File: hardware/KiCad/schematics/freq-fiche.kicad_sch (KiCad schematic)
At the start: 20 parts, among them J1 AudioJack2, J2 AudioJack2, J3 Barrel_Jack_Switch_Pin3Ring, SW1 SW_SPST, SW2 SW_SPST, SW3 SW_SPDT

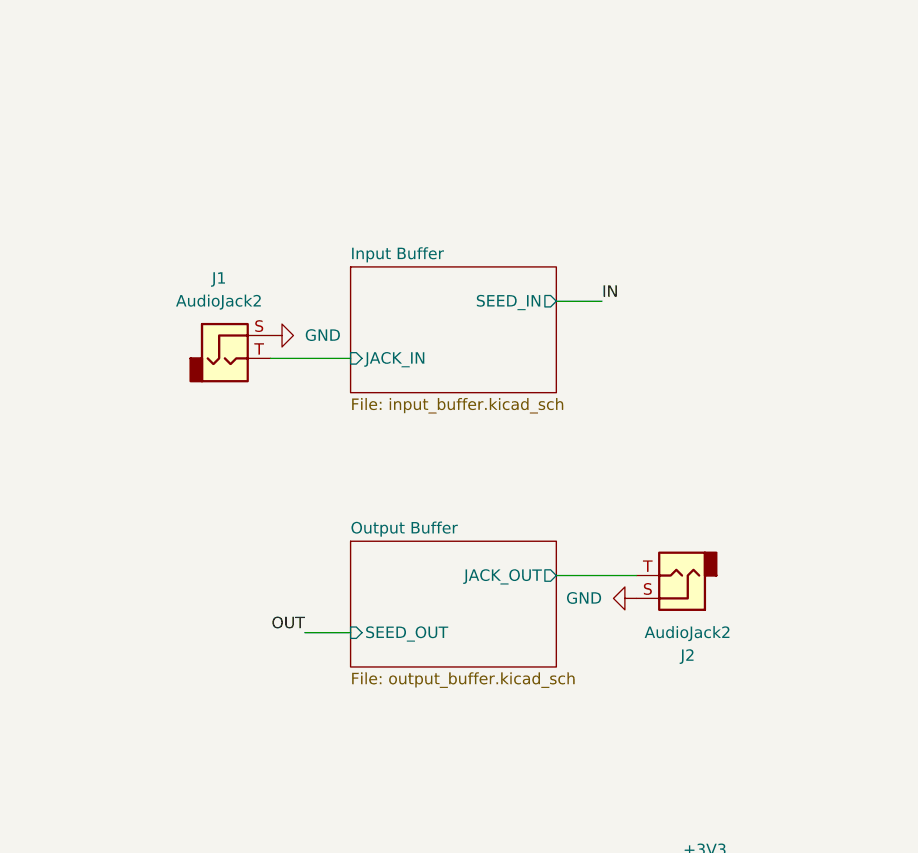
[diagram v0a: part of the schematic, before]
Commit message: Footprint assignments for most components; file organization.
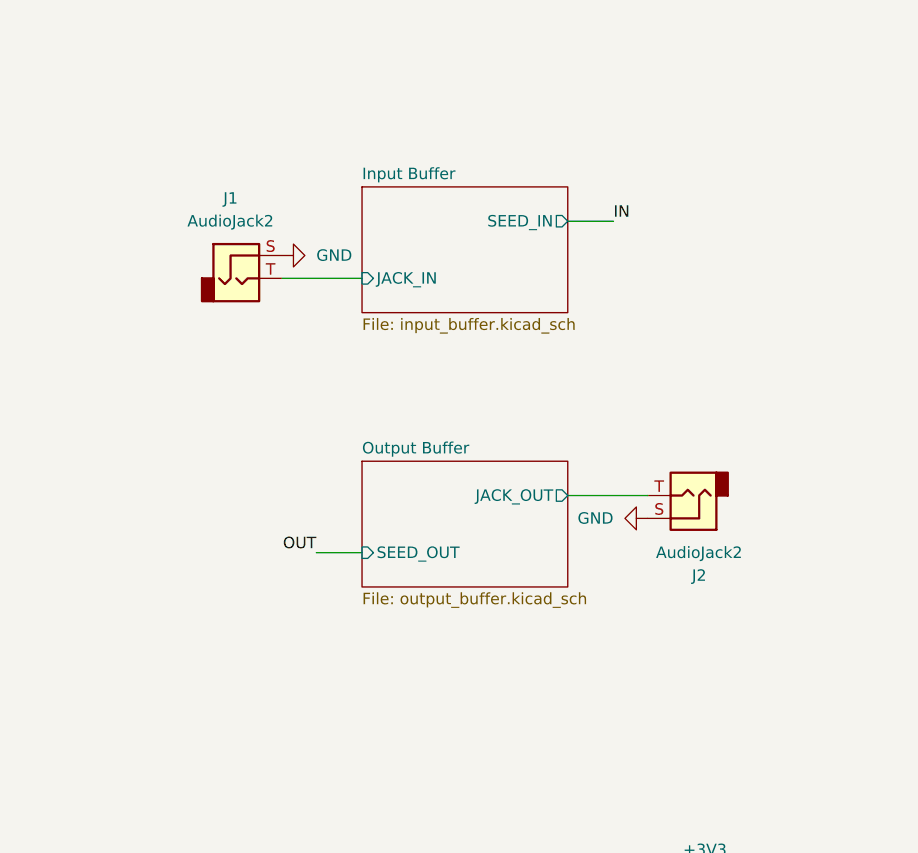
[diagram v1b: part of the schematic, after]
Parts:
- C1: footprint (none) -> Capacitor_THT_Custom:C_Rect_L4.0mm_W2.6mm_P2.50mm
- D1, D2: footprint (none) -> LED_THT:LED_D5.0mm
- J1, J2, SW1, SW2: footprint (none) -> Connector_Wire:SolderWire-0.5sqmm_1x02_P4.6mm_D0.9mm_OD2.1mm
- R1, R2, R3, R4: footprint (none) -> Resistor_THT:R_Axial_DIN0207_L6.3mm_D2.5mm_P7.62mm_Horizontal
- RV1, RV2, RV3, RV4, RV5: footprint (none) -> Potentiometer_THT_Custom:Potentiometer_P160KN
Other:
- moved on the sheet: J1, J2
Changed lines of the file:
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@@
 	(wire
 		(pts
-			(xy 109.22 85.09) (xy 118.11 85.09)
+			(xy 110.49 76.2) (xy 119.38 76.2)
 		)
 		(stroke
@@
 	(wire
 		(pts
-			(xy 81.28 91.44) (xy 86.36 91.44)
+			(xy 82.55 82.55) (xy 87.63 82.55)
 		)
 		(stroke
@@
 	(wire
 		(pts
-			(xy 109.22 54.61) (xy 114.3 54.61)
+			(xy 110.49 45.72) (xy 115.57 45.72)
 		)
 		(stroke
@@
 	(wire
 		(pts
-			(xy 77.47 60.96) (xy 86.36 60.96)
+			(xy 78.74 52.07) (xy 87.63 52.07)
 		)
 		(stroke
@@
 	)
 	(label "IN"
-		(at 114.3 54.61 0)
+		(at 115.57 45.72 0)
 		(effects
 			(font
@@
 	)
 	(label "OUT"
-		(at 81.28 91.44 180)
+		(at 82.55 82.55 180)
 		(effects
 			(font
@@
 			)
 		)
-		(property "Footprint" ""
+		(property "Footprint" "Potentiometer_THT_Custom:Potentiometer_P160KN"
 			(at 116.84 172.72 0)
 			(hide yes)
@@
 			)
 		)
-		(property "Footprint" ""
+		(property "Footprint" "LED_THT:LED_D5.0mm"
 			(at 153.67 138.43 0)
 			(hide yes)
@@
 			)
 		)
-		(property "Footprint" ""
+		(property "Footprint" "Resistor_THT:R_Axial_DIN0207_L6.3mm_D2.5mm_P7.62mm_Horizontal"
 			(at 161.036 126.746 90)
 			(hide yes)
@@
 	(symbol
 		(lib_id "power:GND")
-		(at 118.11 87.63 270)
+		(at 119.38 78.74 270)
 		(unit 1)
 		(body_style 1)
@@
 		(fields_autoplaced yes)
 		(property "Reference" "#PWR06"
-			(at 111.76 87.63 0)
+			(at 113.03 78.74 0)
 			(hide yes)
 			(show_name no)
@@
 		)
 		(property "Value" "GND"
-			(at 114.3 87.6301 90)
+			(at 115.57 78.7401 90)
 			(show_name no)
 			(do_not_autoplace no)
@@
 		)
 		(property "Footprint" ""
-			(at 118.11 87.63 0)
+			(at 119.38 78.74 0)
 			(hide yes)
 			(show_name no)
@@
 		)
 		(property "Datasheet" ""
-			(at 118.11 87.63 0)
+			(at 119.38 78.74 0)
 			(hide yes)
 			(show_name no)
@@
 		)
 		(property "Description" "Power symbol creates a global label with name \"GND\" , ground"
-			(at 118.11 87.63 0)
+			(at 119.38 78.74 0)
 			(hide yes)
 			(show_name no)
@@
 			)
 		)
-		(property "Footprint" ""
+		(property "Footprint" "Resistor_THT:R_Axial_DIN0207_L6.3mm_D2.5mm_P7.62mm_Horizontal"
 			(at 60.706 160.274 90)
 			(hide yes)
@@
 			)
 		)
-		(property "Footprint" ""
+		(property "Footprint" "Resistor_THT:R_Axial_DIN0207_L6.3mm_D2.5mm_P7.62mm_Horizontal"
 			(at 161.544 137.414 90)
 			(hide yes)
@@
 			)
 		)
-		(property "Footprint" ""
+		(property "Footprint" "Potentiometer_THT_Custom:Potentiometer_P160KN"
 			(at 109.22 149.86 0)
 			(hide yes)
@@
 			)
 		)
-		(property "Footprint" ""
+		(property "Footprint" "Capacitor_THT_Custom:C_Rect_L4.0mm_W2.6mm_P2.50mm"
 			(at 54.61 151.4348 0)
 			(hide yes)
@@
 	(symbol
 		(lib_id "Connector_Audio:AudioJack2")
-		(at 123.19 85.09 180)
+		(at 124.46 76.2 180)
 		(unit 1)
 		(body_style 1)
@@
 		(fields_autoplaced yes)
 		(property "Reference" "J2"
-			(at 123.825 93.98 0)
+			(at 125.095 85.09 0)
 			(show_name no)
 			(do_not_autoplace no)
@@
 		)
 		(property "Value" "AudioJack2"
-			(at 123.825 91.44 0)
+			(at 125.095 82.55 0)
 			(show_name no)
 			(do_not_autoplace no)
@@
 			)
 		)
-		(property "Footprint" ""
-			(at 123.19 85.09 0)
+		(property "Footprint" "Connector_Wire:SolderWire-0.5sqmm_1x02_P4.6mm_D0.9mm_OD2.1mm"
+			(at 124.46 76.2 0)
 			(hide yes)
 			(show_name no)
@@
 		)
 		(property "Datasheet" ""
-			(at 123.19 85.09 0)
+			(at 124.46 76.2 0)
 			(hide yes)
 			(show_name no)
@@
 		)
 		(property "Description" "Audio Jack, 2 Poles (Mono / TS)"
-			(at 123.19 85.09 0)
+			(at 124.46 76.2 0)
 			(hide yes)
 			(show_name no)
@@
 			)
 		)
-		(property "Footprint" ""
+		(property "Footprint" "Potentiometer_THT_Custom:Potentiometer_P160KN"
 			(at 113.03 161.29 0)
 			(hide yes)
@@
 			)
 		)
-		(property "Footprint" ""
+		(property "Footprint" "Resistor_THT:R_Axial_DIN0207_L6.3mm_D2.5mm_P7.62mm_Horizontal"
 			(at 60.706 145.034 90)
 			(hide yes)
@@
 			)
 		)
-		(property "Footprint" ""
+		(property "Footprint" "Potentiometer_THT_Custom:Potentiometer_P160KN"
 			(at 101.6 127 0)
 			(hide yes)
@@
 			)
 		)
-		(property "Footprint" ""
+		(property "Footprint" "Connector_Wire:SolderWire-0.5sqmm_1x02_P4.6mm_D0.9mm_OD2.1mm"
 			(at 154.94 152.4 0)
 			(hide yes)
@@
 			)
 		)
-		(property "Footprint" ""
+		(property "Footprint" "LED_THT:LED_D5.0mm"
 			(at 153.67 125.73 0)
 			(hide yes)
@@
 	(symbol
 		(lib_id "Connector_Audio:AudioJack2")
-		(at 72.39 60.96 0)
+		(at 73.66 52.07 0)
 		(unit 1)
 		(body_style 1)
@@
 		(fields_autoplaced yes)
 		(property "Reference" "J1"
-			(at 71.755 52.07 0)
+			(at 73.025 43.18 0)
 			(show_name no)
 			(do_not_autoplace no)
@@
 		)
 		(property "Value" "AudioJack2"
-			(at 71.755 54.61 0)
+			(at 73.025 45.72 0)
 			(show_name no)
 			(do_not_autoplace no)
@@
 			)
 		)
-		(property "Footprint" ""
-			(at 72.39 60.96 0)
+		(property "Footprint" "Connector_Wire:SolderWire-0.5sqmm_1x02_P4.6mm_D0.9mm_OD2.1mm"
+			(at 73.66 52.07 0)
 			(hide yes)
 			(show_name no)
@@
 		)
 		(property "Datasheet" ""
-			(at 72.39 60.96 0)
+			(at 73.66 52.07 0)
 			(hide yes)
 			(show_name no)
@@
 		)
 		(property "Description" "Audio Jack, 2 Poles (Mono / TS)"
-			(at 72.39 60.96 0)
+			(at 73.66 52.07 0)
 			(hide yes)
 			(show_name no)
@@
 			)
 		)
-		(property "Footprint" ""
+		(property "Footprint" "Potentiometer_THT_Custom:Potentiometer_P160KN"
 			(at 105.41 138.43 0)
 			(hide yes)
@@
 			)
 		)
-		(property "Footprint" ""
+		(property "Footprint" "Connector_Wire:SolderWire-0.5sqmm_1x02_P4.6mm_D0.9mm_OD2.1mm"
 			(at 154.94 163.83 0)
 			(hide yes)
@@
 	(symbol
 		(lib_id "power:GND")
-		(at 77.47 58.42 90)
+		(at 78.74 49.53 90)
 		(unit 1)
 		(body_style 1)
@@
 		(fields_autoplaced yes)
 		(property "Reference" "#PWR04"
-			(at 83.82 58.42 0)
+			(at 85.09 49.53 0)
 			(hide yes)
 			(show_name no)
@@
 		)
 		(property "Value" "GND"
-			(at 81.28 58.4199 90)
+			(at 82.55 49.5299 90)
 			(show_name no)
 			(do_not_autoplace no)
@@
 		)
 		(property "Footprint" ""
-			(at 77.47 58.42 0)
+			(at 78.74 49.53 0)
 			(hide yes)
 			(show_name no)
@@
 		)
 		(property "Datasheet" ""
-			(at 77.47 58.42 0)
+			(at 78.74 49.53 0)
 			(hide yes)
 			(show_name no)
@@
 		)
 		(property "Description" "Power symbol creates a global label with name \"GND\" , ground"
-			(at 77.47 58.42 0)
+			(at 78.74 49.53 0)
 			(hide yes)
 			(show_name no)
@@
 	)
 	(sheet
-		(at 86.36 50.8)
+		(at 87.63 41.91)
 		(size 22.86 13.97)
 		(exclude_from_sim no)
@@
 		)
 		(property "Sheetname" "Input Buffer"
-			(at 86.36 50.0884 0)
+			(at 87.63 41.1984 0)
 			(show_name no)
 			(do_not_autoplace no)
@@
 		)
 		(property "Sheetfile" "input_buffer.kicad_sch"
-			(at 86.36 65.3546 0)
+			(at 87.63 56.4646 0)
 			(show_name no)
 			(do_not_autoplace no)
@@
 		)
 		(pin "JACK_IN" input
-			(at 86.36 60.96 180)
+			(at 87.63 52.07 180)
 			(effects
 				(font
@@
 		)
 		(pin "SEED_IN" output
-			(at 109.22 54.61 0)
+			(at 110.49 45.72 0)
 			(effects
 				(font
@@
 	)
 	(sheet
-		(at 86.36 81.28)
+		(at 87.63 72.39)
 		(size 22.86 13.97)
 		(exclude_from_sim no)
@@
 		)
 		(property "Sheetname" "Output Buffer"
-			(at 86.36 80.5684 0)
+			(at 87.63 71.6784 0)
 			(show_name no)
 			(do_not_autoplace no)
@@
 		)
 		(property "Sheetfile" "output_buffer.kicad_sch"
-			(at 86.36 95.8346 0)
+			(at 87.63 86.9446 0)
 			(show_name no)
 			(do_not_autoplace no)
@@
 		)
 		(pin "JACK_OUT" output
-			(at 109.22 85.09 0)
+			(at 110.49 76.2 0)
 			(effects
 				(font
@@
 		)
 		(pin "SEED_OUT" input
-			(at 86.36 91.44 180)
+			(at 87.63 82.55 180)
 			(effects
 				(font

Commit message: Completed initial footprint assignments; courtyard edits.
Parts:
- A1: value Electrosmith_Daisy_Seed_Rev4 -> Electrosmith_Daisy_Seed_Rev7
- J3: footprint (none) -> Connector_Wire_Custom:SolderWire-0.5sqmm_1x03_P4.6mm_D0.9mm_OD2.1mm_BarrelJack
- SW3: footprint (none) -> Connector_Wire_Custom:SolderWire-0.5sqmm_1x03_P4.6mm_D0.9mm_OD2.1mm_SPDT_OnOn
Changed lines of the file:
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@@
 			)
 		)
-		(property "Footprint" ""
+		(property "Footprint" "Connector_Wire_Custom:SolderWire-0.5sqmm_1x03_P4.6mm_D0.9mm_OD2.1mm_BarrelJack"
 			(at 220.98 30.226 0)
 			(hide yes)
@@
 			)
 		)
-		(property "Footprint" ""
+		(property "Footprint" "Connector_Wire_Custom:SolderWire-0.5sqmm_1x03_P4.6mm_D0.9mm_OD2.1mm_SPDT_OnOn"
 			(at 154.94 175.26 0)
 			(hide yes)
@@
 			)
 		)
-		(property "Value" "Electrosmith_Daisy_Seed_Rev4"
+		(property "Value" "Electrosmith_Daisy_Seed_Rev7"
 			(at 234.5533 132.08 0)
 			(show_name no)

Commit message: Added power flags.
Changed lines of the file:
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@@
+	)
+	(junction
+		(at 227.33 55.88)
+		(diameter 0)
+		(color 0 0 0 0)
 	)
 	(junction
@@
 					(unit 1)
 				)
+			)
+		)
+	)
+	(symbol
+		(lib_id "power:PWR_FLAG")
+		(at 227.33 55.88 90)
+		(unit 1)
+		(body_style 1)
+		(exclude_from_sim no)
+		(in_bom yes)
+		(on_board yes)
+		(in_pos_files yes)
+		(dnp no)
+		(fields_autoplaced yes)
+		(property "Reference" "#FLG03"
+			(at 225.425 55.88 0)
+			(hide yes)
+			(show_name no)
+			(do_not_autoplace no)
+			(effects
+				(font
+					(size 1.27 1.27)
+				)
+			)
+		)
+		(property "Value" "PWR_FLAG"
+			(at 223.52 55.8799 90)
+			(show_name no)
+			(do_not_autoplace no)
+			(effects
+				(font
+					(size 1.27 1.27)
+				)
+				(justify left)
+			)
+		)
+		(property "Footprint" ""
+			(at 227.33 55.88 0)
+			(hide yes)
+			(show_name no)
+			(do_not_autoplace no)
+			(effects
+				(font
+					(size 1.27 1.27)
+				)
+			)
+		)
+		(property "Datasheet" ""
+			(at 227.33 55.88 0)
+			(hide yes)
+			(show_name no)
+			(do_not_autoplace no)
+			(effects
+				(font
+					(size 1.27 1.27)
+				)
+			)
+		)
+		(property "Description" "Special symbol for telling ERC where power comes from"
+			(at 227.33 55.88 0)
+			(hide yes)
+			(show_name no)
+			(do_not_autoplace no)
+			(effects
+				(font
+					(size 1.27 1.27)
+				)
+			)
+		)
+		(pin "1"
+		)
+		(instances
+			(project "freq-fiche"
+				(path "/fc444d3c-3a1a-4715-bcff-119f4d2b4d9e"
+					(reference "#FLG03")
+					(unit 1)
+				)

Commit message: Power conditioning.
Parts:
- removed D3: 1N5817, Diode_THT:D_DO-41_SOD81_P10.16mm_Horizontal, symbol Diode:1N5817
- C1: value 0µ1 -> 100n
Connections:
- net +9VCLEAN: now reaches A1.39 (VIN)
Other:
- added sheet Power Conditioner (power_conditioner.kicad_sch)
- moved on the sheet: A1, C1, D1, D2, J1, J2, J3, R1, R2, R3, R4, RV1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
